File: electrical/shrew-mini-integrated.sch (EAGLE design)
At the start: 28 parts, among them U1 ESP32-PICO-D4, U2 SX1280IMLTRT, Y1 52MHz TCXO

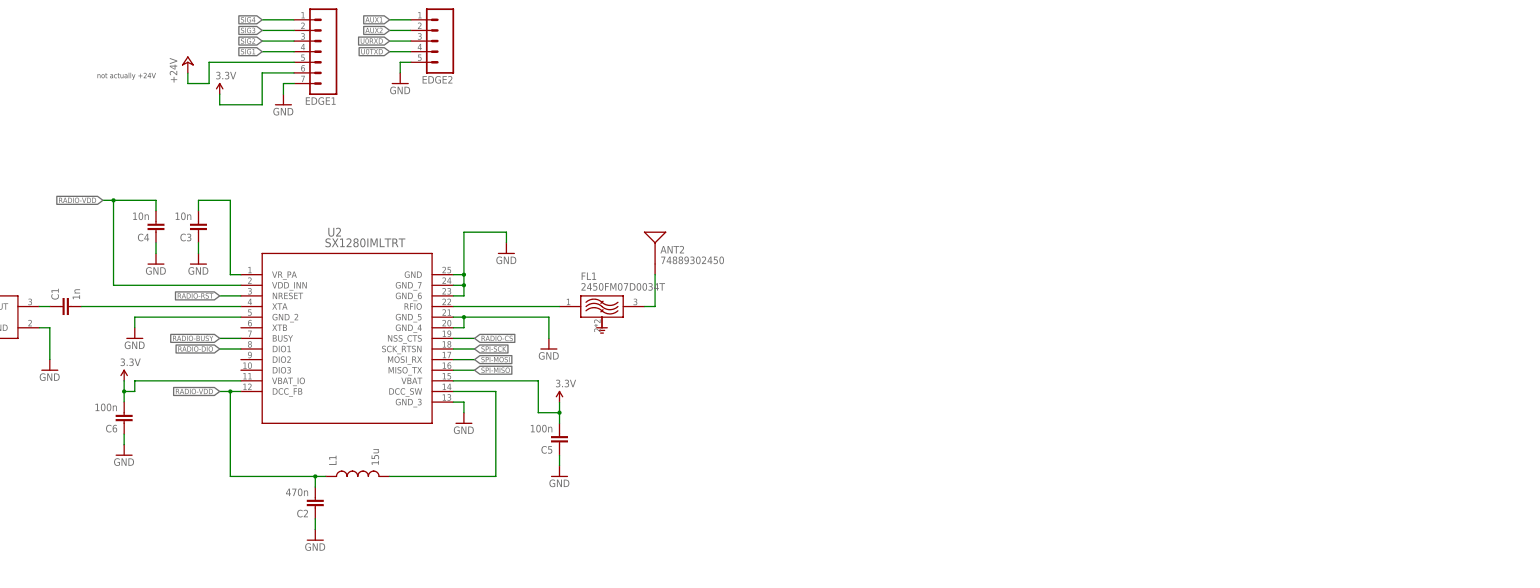
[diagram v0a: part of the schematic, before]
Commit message: initial work on integrated versions
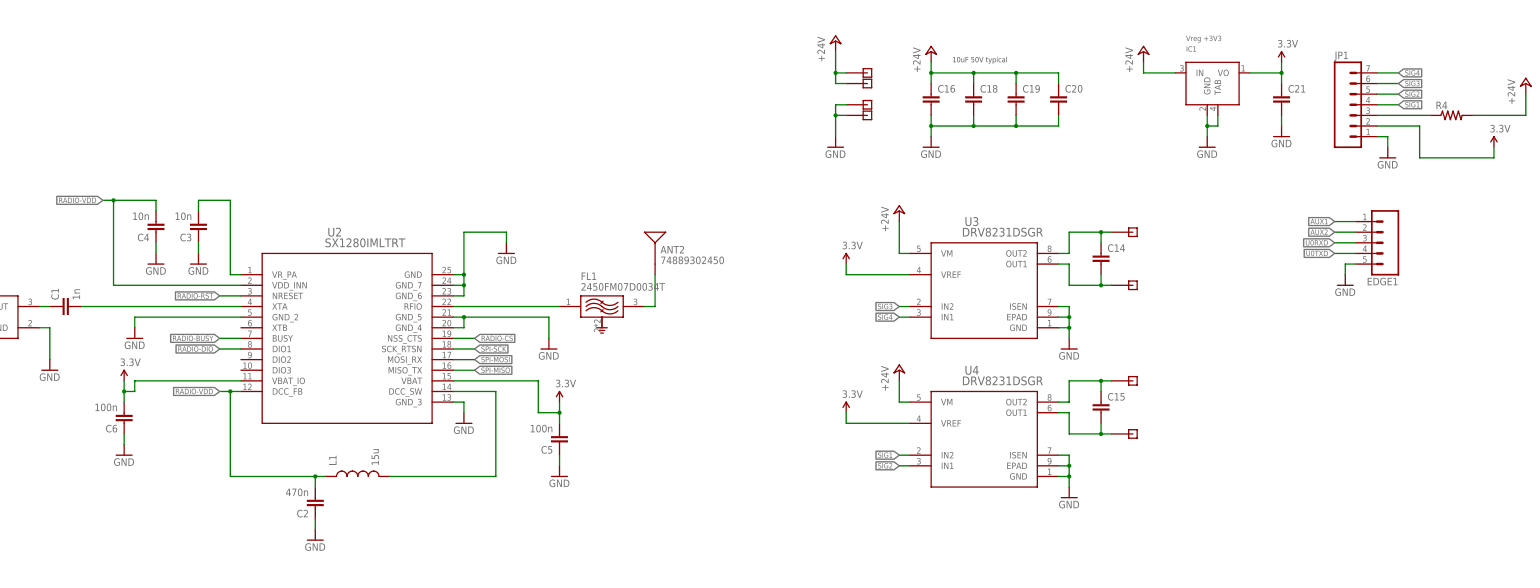
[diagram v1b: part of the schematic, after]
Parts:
- removed EDGE2: (no value), shrew-common:M05PTH
- added C14, C15: (no value), shrew-common:CAP0402-CAP
- added C16, C18, C19, C20, C21: (no value), shrew-common:CAP0805
- added IC1: Vreg +3V3, shrew-common:V_REG_SOT89-SOT89
- added JP1: (no value), shrew-common:M07-2MM-TH-TINY
- added R4: (no value), shrew-common:RESISTOR0402-RES
- added U3, U4: DRV8231DSGR, shrew-core:DRV8231DSGR
- added X1, X2, X3, X4: PIN-1X-BIG, shrew-core:PIN-1X-BIG
- added X5, X6, X7, X8: PIN-1X-MED, shrew-core:PIN-1X-MED
- EDGE1: device shrew-common:M07-2MM-TH -> shrew-common:M05PTH
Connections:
- new net +24V: C16.1, C18.1, C19.1, C20.1, IC1.IN, R4.2, U3.VM, U4.VM, X5.P$1, X7.P$1
- new net MOTOR1: C15.2, U4.OUT1, X3.P$1
- new net MOTOR2: C15.1, U4.OUT2, X4.P$1
- new net MOTOR3: C14.2, U3.OUT1, X1.P$1
- new net MOTOR4: C14.1, U3.OUT2, X2.P$1
- net 3.3V: now also C21.1, IC1.VO, JP1.2, U3.VREF, U4.VREF; no longer EDGE1.6
- net AUX1: now also EDGE1.1; no longer EDGE2.1
- net AUX2: now also EDGE1.2; no longer EDGE2.2
- net GND: now also C16.2, C18.2, C19.2, C20.2, C21.2, EDGE1.5, IC1.GND, IC1.TAB, JP1.1, U3.EPAD, U3.GND, U3.ISEN, U4.EPAD, U4.GND, U4.ISEN, X6.P$1, X8.P$1; no longer EDGE1.7, EDGE2.5
- net SIG1: now also JP1.4, U4.IN2; no longer EDGE1.4
- net SIG2: now also JP1.5, U4.IN1; no longer EDGE1.3
- net SIG3: now also JP1.6, U3.IN2; no longer EDGE1.2
- net SIG4: now also JP1.7, U3.IN1; no longer EDGE1.1
- net U0RXD: now also EDGE1.3; no longer EDGE2.3
- net U0TXD: now also EDGE1.4; no longer EDGE2.4
- net V-ADC: now also JP1.3, R4.1; no longer EDGE1.5
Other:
- note added: "10uF 50V typical"
